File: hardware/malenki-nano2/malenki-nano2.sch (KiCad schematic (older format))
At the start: 22 parts, among them J1 Conn_01x02_Male, J2 Conn_01x04_Male, J5 Conn_01x02_Male, J6 Conn_01x02_Male, J7 Conn_01x02_Male, U1 A7105-MODULE, U2 HT7233, U3 ATtiny3217-M, U5 MX113L, U6 MX113L, U7 MX113L

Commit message: New funky version of the Nano2 board
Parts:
- removed J2: Conn_01x04_Male, Connector_PinHeader_2.00mm:PinHeader_1x04_P2.00mm_Vertical, symbol malenki-nano-rescue:Conn_01x04_Male-Connector
- added J2: Conn_01x03, Connector_PinHeader_2.00mm:PinHeader_1x03_P2.00mm_Vertical, symbol Connector_Generic:Conn_01x03
- added J3: Conn_01x02, malenki-nano:wirepad_2, symbol Connector_Generic:Conn_01x02
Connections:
- net labels added: WEAPON2
- wire segments 56 -> 60
- no-connect marks 10 -> 7
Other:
- note added: "GIO2 was\npreviously connected to\nBLINKY"
- note added: "Servo weapon (Weapon2)"
- note added: "These GPIOs are unused but\nwe tie them to GND for layout"
- note removed: "Note: we drive BLINKY with the GIO pin on the \nradio module, because there are no spare pins\non the MCU"
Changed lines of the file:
@@
 Text GLabel 5600 3400 2    50   Input ~ 0
 UPDI
-$Comp
-L malenki-nano-rescue:Conn_01x04_Male-Connector J2
-U 1 1 5CDCE93F
-P 4900 1800
-F 0 "J2" H 5008 2081 50  0000 C CNN
-F 1 "Conn_01x04_Male" H 5008 1990 50  0000 C CNN
-F 2 "Connector_PinHeader_2.00mm:PinHeader_1x04_P2.00mm_Vertical" H 4900 1800 50  0001 C CNN
-F 3 "~" H 4900 1800 50  0001 C CNN
-	1    4900 1800
-	1    0    0    -1
-$EndComp
 Text Notes 4700 1450 0    50   ~ 0
 Programming / diagnostic
-$Comp
-L malenki-nano-rescue:GND-power #PWR07
-U 1 1 5CDD00E2
-P 6200 2100
-F 0 "#PWR07" H 6200 1850 50  0001 C CNN
-F 1 "GND" H 6205 1927 50  0000 C CNN
-F 2 "" H 6200 2100 50  0001 C CNN
-F 3 "" H 6200 2100 50  0001 C CNN
-	1    6200 2100
-	1    0    0    -1
-$EndComp
-Wire Wire Line
-	5100 1700 6200 1700
-Wire Wire Line
-	6200 1700 6200 2100
 Wire Wire Line
 	5100 1800 5900 1800
@@
 Text GLabel 5100 2000 2    50   Input ~ 0
 UPDI
-Text GLabel 1500 5550 0    50   Input ~ 0
-BLINKY
 Text GLabel 5150 6000 1    50   Input ~ 0
 BLINKY
@@
 	0    -1   -1   0
 $EndComp
-Text Notes 1150 6700 0    50   ~ 0
-Note: we drive BLINKY with the GIO pin on the \nradio module, because there are no spare pins\non the MCU
 $Comp
 L malenki-nano-rescue:C-Device C5
@@
 Text GLabel 5600 3600 2    50   Input ~ 0
 MOTOR1F
-NoConn ~ 5600 4700
 NoConn ~ 5600 4800
 NoConn ~ 5600 4900
@@
 NoConn ~ 4400 4400
 NoConn ~ 4400 4500
-NoConn ~ 4400 4600
-NoConn ~ 4400 4700
-NoConn ~ 4400 4800
 $Comp
 L mal_nano:HT7233 U2
@@
 Wire Wire Line
 	3100 2200 3650 2200
+$Comp
+L malenki-nano-rescue:GND-power #PWR0101
+U 1 1 5DC6F674
+P 3600 4800
+F 0 "#PWR0101" H 3600 4550 50  0001 C CNN
+F 1 "GND" H 3605 4627 50  0000 C CNN
+F 2 "" H 3600 4800 50  0001 C CNN
+F 3 "" H 3600 4800 50  0001 C CNN
+	1    3600 4800
+	1    0    0    -1
+$EndComp
+Wire Wire Line
+	4400 4700 3600 4700
+Wire Wire Line
+	3600 4700 3600 4800
+Text Notes 3200 4550 0    50   ~ 0
+These GPIOs are unused but\nwe tie them to GND for layout
+$Comp
+L Connector_Generic:Conn_01x03 J2
+U 1 1 5E297C26
+P 4900 1900
+F 0 "J2" H 4818 2217 50  0000 C CNN
+F 1 "Conn_01x03" H 4818 2126 50  0000 C CNN
+F 2 "Connector_PinHeader_2.00mm:PinHeader_1x03_P2.00mm_Vertical" H 4900 1900 50  0001 C CNN
+F 3 "~" H 4900 1900 50  0001 C CNN
+	1    4900 1900
+	-1   0    0    -1
+$EndComp
+$Comp
+L Connector_Generic:Conn_01x02 J3
+U 1 1 5E29E95E
+P 6850 1950
+F 0 "J3" H 6930 1942 50  0000 L CNN
+F 1 "Conn_01x02" H 6930 1851 50  0000 L CNN
+F 2 "malenki-nano:wirepad_2" H 6850 1950 50  0001 C CNN
+F 3 "~" H 6850 1950 50  0001 C CNN
+	1    6850 1950
+	1    0    0    -1
+$EndComp
+Text Notes 6450 1750 0    50   ~ 0
+Servo weapon (Weapon2)
+$Comp
+L malenki-nano-rescue:GND-power #PWR0102
+U 1 1 5E2A31C0
+P 6400 2100
+F 0 "#PWR0102" H 6400 1850 50  0001 C CNN
+F 1 "GND" H 6405 1927 50  0000 C CNN
+F 2 "" H 6400 2100 50  0001 C CNN
+F 3 "" H 6400 2100 50  0001 C CNN
+	1    6400 2100
+	1    0    0    -1
+$EndComp
+Wire Wire Line
+	6650 2050 6400 2050
+Wire Wire Line
+	6400 2050 6400 2100
+Text GLabel 6650 1950 0    50   Input ~ 0
+WEAPON2
+Text GLabel 5600 4700 2    50   Input ~ 0
+WEAPON2
+NoConn ~ 1500 5550
+Text GLabel 4400 4800 0    50   Input ~ 0
+BLINKY
+Wire Wire Line
+	3600 4600 3600 4700
+Wire Wire Line
+	3600 4600 4400 4600
+Connection ~ 3600 4700
+Text Notes 500  5650 0    50   ~ 0
+GIO2 was\npreviously connected to\nBLINKY
 $EndSCHEMATC

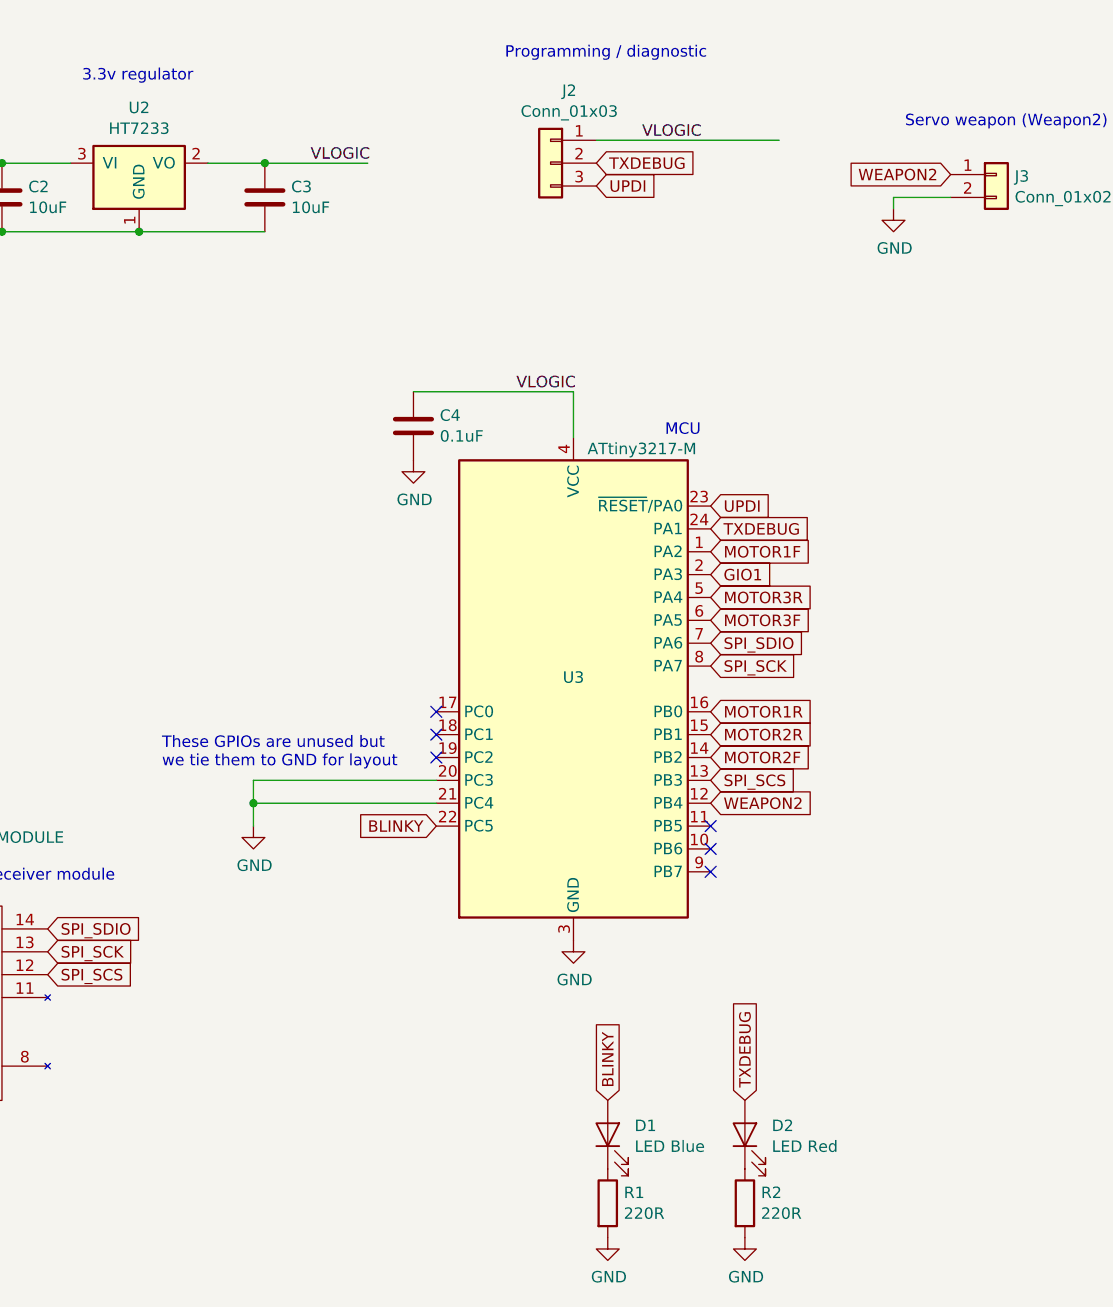
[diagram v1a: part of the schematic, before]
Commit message: move resistor to back side for assembly
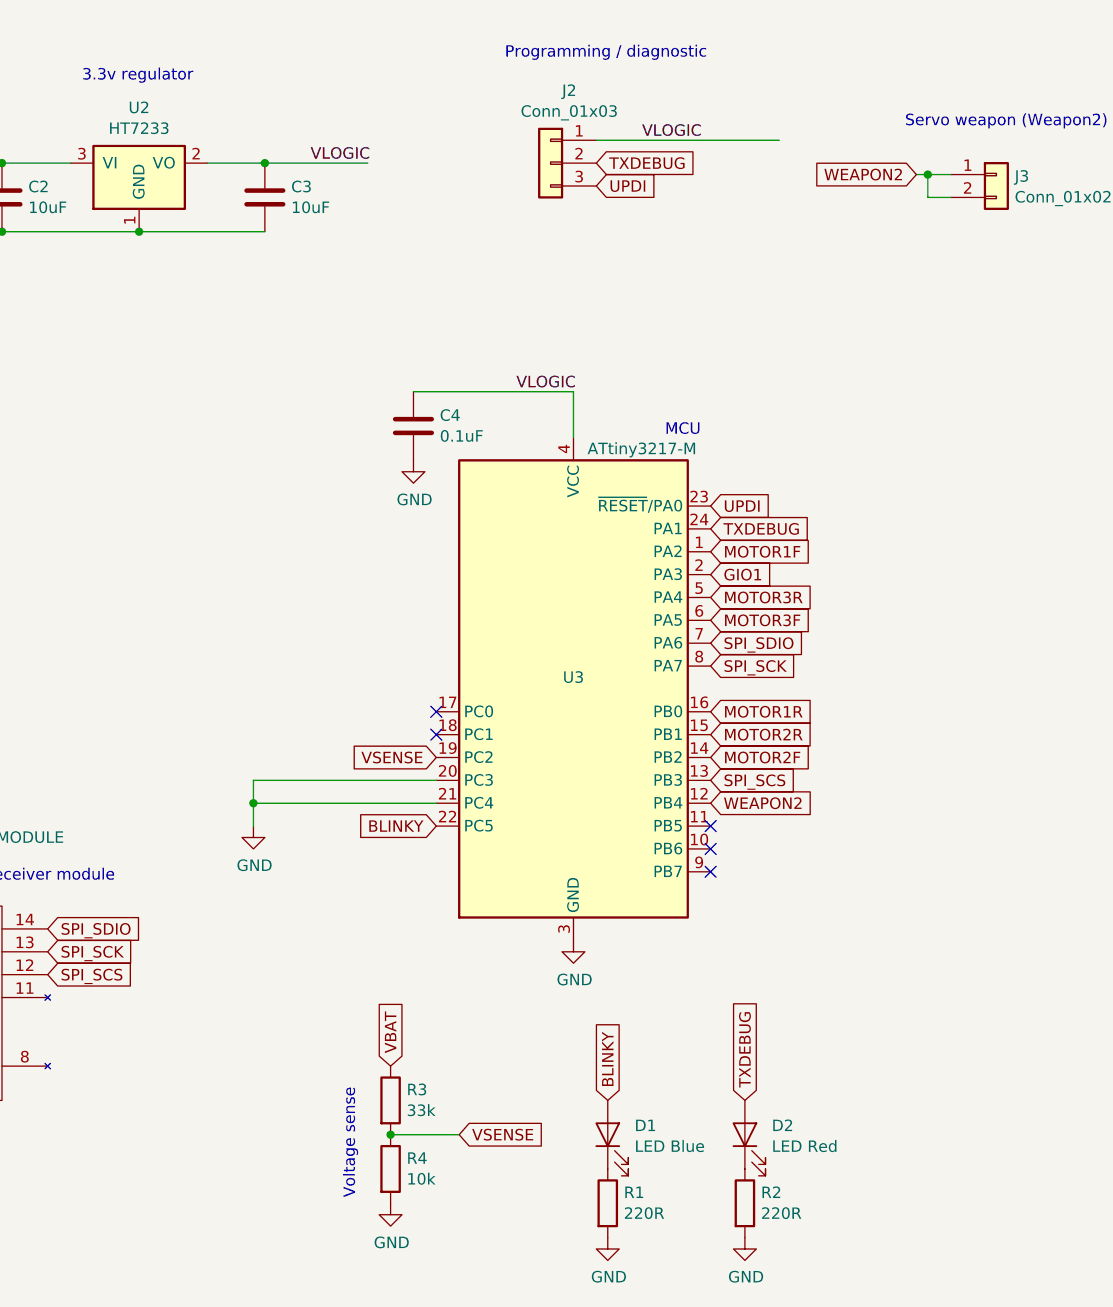
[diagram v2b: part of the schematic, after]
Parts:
- added R3: 33k, Resistor_SMD:R_0603_1608Metric, symbol malenki-nano-rescue:R-Device
- added R4: 10k, Resistor_SMD:R_0603_1608Metric, symbol malenki-nano-rescue:R-Device
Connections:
- net labels added: VSENSE
- wire segments 60 -> 63
- no-connect marks 7 -> 6
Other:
- note added: "Voltage sense"
- note removed: "These GPIOs are unused but\nwe tie them to GND for layout"
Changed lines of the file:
@@
 NoConn ~ 4400 4300
 NoConn ~ 4400 4400
-NoConn ~ 4400 4500
 $Comp
 L mal_nano:HT7233 U2
@@
 Wire Wire Line
 	3600 4700 3600 4800
-Text Notes 3200 4550 0    50   ~ 0
-These GPIOs are unused but\nwe tie them to GND for layout
 $Comp
 L Connector_Generic:Conn_01x03 J2
@@
 Text Notes 6450 1750 0    50   ~ 0
 Servo weapon (Weapon2)
-$Comp
-L malenki-nano-rescue:GND-power #PWR0102
-U 1 1 5E2A31C0
-P 6400 2100
-F 0 "#PWR0102" H 6400 1850 50  0001 C CNN
-F 1 "GND" H 6405 1927 50  0000 C CNN
-F 2 "" H 6400 2100 50  0001 C CNN
-F 3 "" H 6400 2100 50  0001 C CNN
-	1    6400 2100
-	1    0    0    -1
-$EndComp
-Wire Wire Line
-	6650 2050 6400 2050
-Wire Wire Line
-	6400 2050 6400 2100
-Text GLabel 6650 1950 0    50   Input ~ 0
+Text GLabel 6500 1950 0    50   Input ~ 0
 WEAPON2
 Text GLabel 5600 4700 2    50   Input ~ 0
@@
 Text Notes 500  5650 0    50   ~ 0
 GIO2 was\npreviously connected to\nBLINKY
+Wire Wire Line
+	6650 1950 6550 1950
+Wire Wire Line
+	6650 2050 6550 2050
+Wire Wire Line
+	6550 2050 6550 1950
+Connection ~ 6550 1950
+Wire Wire Line
+	6550 1950 6500 1950
+Text GLabel 4400 4500 0    50   Input ~ 0
+VSENSE
+Text GLabel 4500 6150 2    50   Input ~ 0
+VSENSE
+$Comp
+L malenki-nano-rescue:R-Device R3
+U 1 1 5E302ABB
+P 4200 6000
+F 0 "R3" H 4270 6046 50  0000 L CNN
+F 1 "33k" H 4270 5955 50  0000 L CNN
+F 2 "Resistor_SMD:R_0603_1608Metric" V 4130 6000 50  0001 C CNN
+F 3 "~" H 4200 6000 50  0001 C CNN
+	1    4200 6000
+	1    0    0    -1
+$EndComp
+$Comp
+L malenki-nano-rescue:R-Device R4
+U 1 1 5E305615
+P 4200 6300
+F 0 "R4" H 4270 6346 50  0000 L CNN
+F 1 "10k" H 4270 6255 50  0000 L CNN
+F 2 "Resistor_SMD:R_0603_1608Metric" V 4130 6300 50  0001 C CNN
+F 3 "~" H 4200 6300 50  0001 C CNN
+	1    4200 6300
+	1    0    0    -1
+$EndComp
+Wire Wire Line
+	4500 6150 4200 6150
+Connection ~ 4200 6150
+$Comp
+L malenki-nano-rescue:GND-power #PWR07
+U 1 1 5E309C5A
+P 4200 6450
+F 0 "#PWR07" H 4200 6200 50  0001 C CNN
+F 1 "GND" H 4205 6277 50  0000 C CNN
+F 2 "" H 4200 6450 50  0001 C CNN
+F 3 "" H 4200 6450 50  0001 C CNN
+	1    4200 6450
+	1    0    0    -1
+$EndComp
+Text GLabel 4200 5850 1    50   Input ~ 0
+VBAT
+Text Notes 4050 5950 3    50   ~ 0
+Voltage sense
 $EndSCHEMATC

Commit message: move around again
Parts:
- C1, C4: LCSC (none) -> C14663; Partnum (none) -> C14663
- C2, C3, C5, C6, C7: LCSC (none) -> C96446; Partnum (none) -> C96446
- D1: footprint LED_SMD:LED_1206_3216Metric_Castellated -> LED_SMD:LED_0805_2012Metric_Castellated; LCSC (none) -> C2293
- D2: footprint LED_SMD:LED_1206_3216Metric_Castellated -> LED_SMD:LED_0805_2012Metric_Castellated; LCSC (none) -> C84256
- R1, R2: LCSC (none) -> C22962; Partnum (none) -> C22962
- R3: LCSC (none) -> C4216; Partnum (none) -> C4216
- R4: LCSC (none) -> C25804; Partnum (none) -> C25804
- U2: LCSC (none) -> C211659; Partnum (none) -> C211659
- U3: value ATtiny3217-M -> ATtiny1617-M; symbol MCU_Microchip_ATtiny:ATtiny3217-M -> MCU_Microchip_ATtiny:ATtiny1617-M; LCSC (none) -> C194193; Partnum (none) -> C194193
- U5, U6, U7: LCSC (none) -> C182096
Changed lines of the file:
@@
 F 2 "Capacitor_SMD:C_0603_1608Metric" H 2538 1900 50  0001 C CNN
 F 3 "~" H 2500 2050 50  0001 C CNN
+F 4 "C96446" H 2500 2050 50  0001 C CNN "Partnum"
+F 5 "C96446" H 2500 2050 50  0001 C CNN "LCSC"
 	1    2500 2050
 	1    0    0    -1
@@
 F 2 "Capacitor_SMD:C_0603_1608Metric" H 3688 1900 50  0001 C CNN
 F 3 "~" H 3650 2050 50  0001 C CNN
+F 4 "C96446" H 3650 2050 50  0001 C CNN "Partnum"
+F 5 "C96446" H 3650 2050 50  0001 C CNN "LCSC"
 	1    3650 2050
 	1    0    0    -1
@@
 F 2 "Capacitor_SMD:C_0603_1608Metric" H 1438 4650 50  0001 C CNN
 F 3 "~" H 1400 4800 50  0001 C CNN
+F 4 "C14663" H 1400 4800 50  0001 C CNN "Partnum"
+F 5 "C14663" H 1400 4800 50  0001 C CNN "LCSC"
 	1    1400 4800
 	1    0    0    -1
@@
 F 2 "Resistor_SMD:R_0603_1608Metric" V 5080 6450 50  0001 C CNN
 F 3 "~" H 5150 6450 50  0001 C CNN
+F 4 "C22962" H 5150 6450 50  0001 C CNN "Partnum"
+F 5 "C22962" H 5150 6450 50  0001 C CNN "LCSC"
 	1    5150 6450
 	1    0    0    -1
@@
 F 0 "D1" V 5189 6033 50  0000 R CNN
 F 1 "LED Blue" V 5098 6033 50  0000 R CNN
-F 2 "LED_SMD:LED_1206_3216Metric_Castellated" H 5150 6150 50  0001 C CNN
+F 2 "LED_SMD:LED_0805_2012Metric_Castellated" H 5150 6150 50  0001 C CNN
 F 3 "~" H 5150 6150 50  0001 C CNN
+F 4 "C2293" H 5150 6150 50  0001 C CNN "LCSC"
 	1    5150 6150
 	0    -1   -1   0
@@
 F 2 "Capacitor_SMD:C_0603_1608Metric" H 8688 1700 50  0001 C CNN
 F 3 "~" H 8650 1850 50  0001 C CNN
+F 4 "C96446" H 8650 1850 50  0001 C CNN "Partnum"
+F 5 "C96446" H 8650 1850 50  0001 C CNN "LCSC"
 	1    8650 1850
 	1    0    0    -1
@@
 F 2 "Capacitor_SMD:C_0603_1608Metric" H 8488 3750 50  0001 C CNN
 F 3 "~" H 8450 3900 50  0001 C CNN
+F 4 "C96446" H 8450 3900 50  0001 C CNN "Partnum"
+F 5 "C96446" H 8450 3900 50  0001 C CNN "LCSC"
 	1    8450 3900
 	1    0    0    -1
@@
 F 2 "Capacitor_SMD:C_0603_1608Metric" H 8688 5700 50  0001 C CNN
 F 3 "~" H 8650 5850 50  0001 C CNN
+F 4 "C96446" H 8650 5850 50  0001 C CNN "Partnum"
+F 5 "C96446" H 8650 5850 50  0001 C CNN "LCSC"
 	1    8650 5850
 	1    0    0    -1
@@
 F 2 "Resistor_SMD:R_0603_1608Metric" V 5680 6450 50  0001 C CNN
 F 3 "~" H 5750 6450 50  0001 C CNN
+F 4 "C22962" H 5750 6450 50  0001 C CNN "Partnum"
+F 5 "C22962" H 5750 6450 50  0001 C CNN "LCSC"
 	1    5750 6450
 	1    0    0    -1
@@
 F 0 "D2" V 5789 6033 50  0000 R CNN
 F 1 "LED Red" V 5698 6033 50  0000 R CNN
-F 2 "LED_SMD:LED_1206_3216Metric_Castellated" H 5750 6150 50  0001 C CNN
+F 2 "LED_SMD:LED_0805_2012Metric_Castellated" H 5750 6150 50  0001 C CNN
 F 3 "~" H 5750 6150 50  0001 C CNN
+F 4 "C84256" H 5750 6150 50  0001 C CNN "LCSC"
 	1    5750 6150
 	0    -1   -1   0
@@
 F 2 "Package_TO_SOT_SMD:SOT-23-6" H 9400 1150 50  0001 C CNN
 F 3 "" H 9400 1150 50  0001 C CNN
+F 4 "C182096" H 9400 1150 50  0001 C CNN "LCSC"
 	1    9400 1150
 	1    0    0    -1
@@
 F 2 "Package_TO_SOT_SMD:SOT-23-6" H 9300 3250 50  0001 C CNN
 F 3 "" H 9300 3250 50  0001 C CNN
+F 4 "C182096" H 9300 3250 50  0001 C CNN "LCSC"
 	1    9300 3250
 	1    0    0    -1
@@
 F 2 "Package_TO_SOT_SMD:SOT-23-6" H 9550 5250 50  0001 C CNN
 F 3 "" H 9550 5250 50  0001 C CNN
+F 4 "C182096" H 9550 5250 50  0001 C CNN "LCSC"
 	1    9550 5250
 	1    0    0    -1
@@
 	8500 5700 8400 5700
 $Comp
-L MCU_Microchip_ATtiny:ATtiny3217-M U3
+L MCU_Microchip_ATtiny:ATtiny1617-M U3
 U 1 1 5DC45560
 P 5000 4200
 F 0 "U3" H 5000 4250 50  0000 C CNN
-F 1 "ATtiny3217-M" H 5300 5250 50  0000 C CNN
+F 1 "ATtiny1617-M" H 5300 5250 50  0000 C CNN
 F 2 "malenki-nano:qfn24-hand1" H 5000 4200 50  0001 C CIN
 F 3 "http://ww1.microchip.com/downloads/en/DeviceDoc/ATtiny3217_1617-Data-Sheet-40001999B.pdf" H 5000 4200 50  0001 C CNN
+F 4 "C194193" H 5000 4200 50  0001 C CNN "Partnum"
+F 5 "C194193" H 5000 4200 50  0001 C CNN "LCSC"
 	1    5000 4200
 	1    0    0    -1
@@
 F 2 "Capacitor_SMD:C_0603_1608Metric" H 4338 2900 50  0001 C CNN
 F 3 "~" H 4300 3050 50  0001 C CNN
+F 4 "C14663" H 4300 3050 50  0001 C CNN "Partnum"
+F 5 "C14663" H 4300 3050 50  0001 C CNN "LCSC"
 	1    4300 3050
 	1    0    0    -1
@@
 F 2 "Package_TO_SOT_SMD:SOT-23" H 3100 1750 50  0001 C CNN
 F 3 "https://datasheet.lcsc.com/szlcsc/1809191917_Holtek-Semicon-HT7233_C47970.pdf" H 3100 1750 50  0001 C CNN
+F 4 "C211659" H 3100 1750 50  0001 C CNN "Partnum"
+F 5 "C211659" H 3100 1750 50  0001 C CNN "LCSC"
 	1    3100 1750
 	1    0    0    -1
@@
 F 2 "Resistor_SMD:R_0603_1608Metric" V 4130 6000 50  0001 C CNN
 F 3 "~" H 4200 6000 50  0001 C CNN
+F 4 "C4216" H 4200 6000 50  0001 C CNN "Partnum"
+F 5 "C4216" H 4200 6000 50  0001 C CNN "LCSC"
 	1    4200 6000
 	1    0    0    -1
@@
 F 2 "Resistor_SMD:R_0603_1608Metric" V 4130 6300 50  0001 C CNN
 F 3 "~" H 4200 6300 50  0001 C CNN
+F 4 "C25804" H 4200 6300 50  0001 C CNN "Partnum"
+F 5 "C25804" H 4200 6300 50  0001 C CNN "LCSC"
 	1    4200 6300
 	1    0    0    -1

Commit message: various updates and drv8837 breakout
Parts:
- C2, C3, C5, C6, C7: LCSC C96446 -> C19702; Partnum C96446 -> (none)
- D1: LCSC C2293 -> C72035
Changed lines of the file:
@@
 F 2 "Capacitor_SMD:C_0603_1608Metric" H 2538 1900 50  0001 C CNN
 F 3 "~" H 2500 2050 50  0001 C CNN
-F 4 "C96446" H 2500 2050 50  0001 C CNN "Partnum"
-F 5 "C96446" H 2500 2050 50  0001 C CNN "LCSC"
+F 4 "" H 2500 2050 50  0001 C CNN "Partnum"
+F 5 "C19702" H 2500 2050 50  0001 C CNN "LCSC"
 	1    2500 2050
 	1    0    0    -1
@@
 F 2 "Capacitor_SMD:C_0603_1608Metric" H 3688 1900 50  0001 C CNN
 F 3 "~" H 3650 2050 50  0001 C CNN
-F 4 "C96446" H 3650 2050 50  0001 C CNN "Partnum"
-F 5 "C96446" H 3650 2050 50  0001 C CNN "LCSC"
+F 4 "" H 3650 2050 50  0001 C CNN "Partnum"
+F 5 "C19702" H 3650 2050 50  0001 C CNN "LCSC"
 	1    3650 2050
 	1    0    0    -1
@@
 F 2 "LED_SMD:LED_0805_2012Metric_Castellated" H 5150 6150 50  0001 C CNN
 F 3 "~" H 5150 6150 50  0001 C CNN
-F 4 "C2293" H 5150 6150 50  0001 C CNN "LCSC"
+F 4 "C72035" H 5150 6150 50  0001 C CNN "LCSC"
 	1    5150 6150
 	0    -1   -1   0
@@
 F 2 "Capacitor_SMD:C_0603_1608Metric" H 8688 1700 50  0001 C CNN
 F 3 "~" H 8650 1850 50  0001 C CNN
-F 4 "C96446" H 8650 1850 50  0001 C CNN "Partnum"
-F 5 "C96446" H 8650 1850 50  0001 C CNN "LCSC"
+F 4 "" H 8650 1850 50  0001 C CNN "Partnum"
+F 5 "C19702" H 8650 1850 50  0001 C CNN "LCSC"
 	1    8650 1850
 	1    0    0    -1
@@
 F 2 "Capacitor_SMD:C_0603_1608Metric" H 8488 3750 50  0001 C CNN
 F 3 "~" H 8450 3900 50  0001 C CNN
-F 4 "C96446" H 8450 3900 50  0001 C CNN "Partnum"
-F 5 "C96446" H 8450 3900 50  0001 C CNN "LCSC"
+F 4 "" H 8450 3900 50  0001 C CNN "Partnum"
+F 5 "C19702" H 8450 3900 50  0001 C CNN "LCSC"
 	1    8450 3900
 	1    0    0    -1
@@
 F 2 "Capacitor_SMD:C_0603_1608Metric" H 8688 5700 50  0001 C CNN
 F 3 "~" H 8650 5850 50  0001 C CNN
-F 4 "C96446" H 8650 5850 50  0001 C CNN "Partnum"
-F 5 "C96446" H 8650 5850 50  0001 C CNN "LCSC"
+F 4 "" H 8650 5850 50  0001 C CNN "Partnum"
+F 5 "C19702" H 8650 5850 50  0001 C CNN "LCSC"
 	1    8650 5850
 	1    0    0    -1

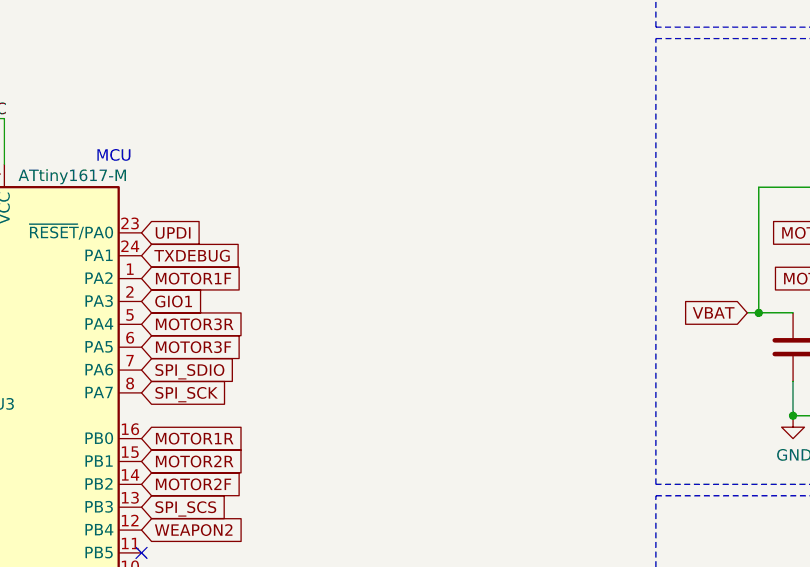
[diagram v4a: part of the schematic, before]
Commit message: note design error
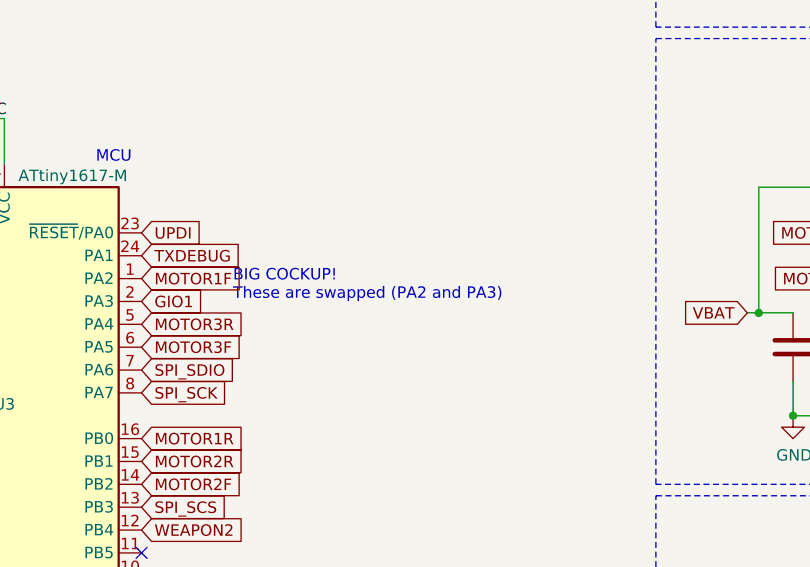
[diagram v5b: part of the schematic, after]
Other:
- note added: "BIG COCKUP!\nThese are swapped (PA2 and PA3)"
